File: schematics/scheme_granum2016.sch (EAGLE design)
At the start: 42 parts, among them M1 SMALL_SERVO, U1 TSL2561T, U2 TSL2561T, U3 TSL2561T

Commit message: добавляем в пояснительную записку описание измерительного моста + в схеме подключен мост, термисторы и немного по мелочам Гранум, с наступающим!
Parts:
- removed LSP10, LSP12, LSP13, LSP14, LSP15, LSP16, LSP2, LSP3, LSP4, LSP8, LSP9: LSP10, solpad:LSP10
- removed R8, R9: PTC-SOD70, ptc-ntc:PTC-SOD70
- removed X2: (no value), con-molex:KK-156-8
- added 3.3V_1, 5V_1, 5V_2, 5V_3, ADDR_LS1, ADDR_LS2, ADDR_LS3, BZZR, CMN1, CMN2, CMN3, CS_ADXL, CS_DP, DHT, EN_MP1, EN_MP2, EN_MP3, GND1_1, GND2_2, GND3_3, INT1, INT2, INT_LS1, INT_LS2, INT_LS3, NTC1, NTC2, NTC3, SCL, SDA, SERVO, SOIL1, SOIL2: LSP10, solpad:LSP10
- added R11, R13: PTC-SOD70, ptc-ntc:PTC-SOD70
- added R12, R14: (no value), eagle-ltspice:R0207/10
- renumbered LSP5 to CS_MP1, LSP6 to CS_MP2, LSP7 to CS_MP3
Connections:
- removed net N$9: U3.VDD
- new net +3V3: U$1.VIO, U$1.VS, U$2.VDD, U$7.VDD, U1.VDD, U2.VDD, U3.VDD
- new net +5V: M1.V+, U$3.VCC, U$3.VH/RH, U$4.VCC, U$4.Y0, U$5.VCC, U$5.Y0, U$6.VCC, U$6.Y0, U4.VDD
- new net 3.3V_1: 3.3V_1.MP
- new net 5V_1: 5V_1.MP, R12.1, R14.1, R5.1
- new net 5V_2: 5V_2.MP
- new net 5V_3: 5V_3.MP
- new net GND1: GND1_1.MP, R10.1
- new net GND2: GND2_2.MP, R11.1
- new net GND3: GND3_3.MP, R13.1
- new net N$22: R6.2, SOIL1.MP, U$4.Y1, U$5.Y1, U$6.Y1
- new net N$24: CMN1.MP, U$5.Z
- new net N$26: NTC2.MP, R12.2, U$7.A1
- new net N$28: R7.2, SOIL2.MP, U$3.VW/RW
- new net N$30: NTC3.MP, R14.2, U$7.A2
- new net N$31: CMN2.MP, U$6.Z
- new net N$32: CMN3.MP, U$4.Z
- net 3.3V: no longer U$2.VDD, U1.VDD, U2.VDD
- net 5V: no longer M1.V+, U4.VDD
- net GND: now also R6.1, R7.1, U$3.VL/RL, U$3.VSS
- net N$13: now also EN_MP2.MP; no longer LSP9.MP
- net N$14: now also EN_MP3.MP; no longer LSP10.MP
- net N$16: now also EN_MP1.MP; no longer LSP8.MP
- net N$17: now also INT_LS3.MP; no longer LSP12.MP
- net N$18: now also BZZR.MP
- net N$19: now also DHT.MP
- net N$2: now also INT1.MP; no longer LSP3.MP
- net N$20: now also NTC1.MP, R5.2, U$7.A0; no longer U$7.VDD
- net N$21: now also INT_LS2.MP; no longer LSP15.MP
- net N$23: now also ADDR_LS2.MP; no longer LSP13.MP
- net N$25: now also SERVO.MP
- net N$27: now also INT_LS1.MP; no longer LSP16.MP
- net N$29: now also ADDR_LS1.MP; no longer LSP14.MP
- net N$3: now also SCL.MP; no longer X2-1.S
- net N$4: now also INT2.MP; no longer LSP2.MP
- net N$5: now also CS_DP.MP, U$3.CS; no longer U$1.CS, U$1.VIO, U$1.VS
- net N$6: now also ADDR_LS3.MP; no longer LSP4.MP
- net N$7: now also SDA.MP; no longer X2-2.S
- net N$8: now also CS_ADXL.MP, U$1.CS; no longer U$4.VCC, U$5.VCC, U$6.VCC
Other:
- moved on the sheet: LSP1, LSP11, R10, R5, R6, R7, SG1, U1, U2, U3, U4

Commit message: в ПЗ добавлено описание измерения твердости, в презентации изменено расширение видео, в схемах теперь подключены STM32, microSD & GPS, в библиотеке есть ATmega128
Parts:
- removed 5V_1, 5V_2, 5V_3, GND3_3: LSP10, solpad:LSP10
- added 3.3V_2, 3.3V_3, 5V_1_1, 5V_1_2, 5V_2_1, 5V_2_2, 5V_3_1, 5V_3_2, GND1_2, GND2_1, GND3_1, GND3_2: LSP10, solpad:LSP10
- added U$10: MICRO_SD, elements_cs2016:MICRO_SD
- added U$11: ATMEGA128, elements_cs2016:ATMEGA128
- added U$8: STM32, elements_cs2016:STM32
- added U$9: GPS, elements_cs2016:GPS
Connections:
- removed net +3V3: U$1.VIO, U$1.VS, U$2.VDD, U$7.VDD, U1.VDD, U2.VDD, U3.VDD
- removed net 5V_1: 5V_1.MP, R12.1, R14.1, R5.1
- removed net 5V_2: 5V_2.MP
- removed net 5V_3: 5V_3.MP
- removed net GND1: GND1_1.MP, R10.1
- removed net GND2: GND2_2.MP, R11.1
- removed net GND3: GND3_3.MP, R13.1
- new net 3.3V_2: 3.3V_2.MP, U$1.SDO, U$1.VIO, U$1.VS, U$7.VDD, U2.VDD
- new net 3.3V_3: 3.3V_3.MP, U$8.3.3V, U$9.VCC, U1.VDD
- new net 5V11: 5V_1_1.MP, R5.1
- new net 5V12: 5V_1_2.MP
- new net 5V21: 5V_2_1.MP, R12.1, U4.VDD
- new net 5V22: 5V_2_2.MP, M1.V+
- new net 5V31: 5V_3_1.MP, R14.1, U$8.5V
- new net 5V32: 5V_3_2.MP, U$10.VCC
- new net GND11: GND1_1.MP, R10.1, U$2.GND
- new net GND12: GND1_2.MP, SG1.-, U3.GND
- new net GND21: GND2_1.MP, M1.GND, R11.1, U$1.GND, U$11.GND1, U$11.GND2, U4.GND
- new net GND22: GND2_2.MP, U$11.GND, U$7.GND, U2.GND
- new net GND31: GND3_1.MP, R13.1, U$10.GND, U$8.G, U$8.GN, U$8.GNDD, U$9.GND
- new net GND32: GND3_2.MP, U1.GND
- new net N$33: U$8.B6, U$9.RX
- new net N$34: U$10.MISO, U$8.A6
- new net N$35: U$10.MOSI, U$8.A7
- new net N$36: U$10.SCK, U$8.A5
- new net N$37: U$10.CS, U$8.A4
- new net N$9: U$8.B7, U$9.TX
- new net SCL: SCL.MP, U$11.(SCL/INT0)PD0, U2.SCL, U3.SCL
- new net SDA: SDA.MP, U$11.(SDA/INT1)PD1, U2.SDA, U3.SDA
- new net SDA_3,3V: U$1.SDA
- net +5V: no longer M1.V+, U4.VDD
- net 3.3V: no longer U$1.SDO
- net 3.3V_1: now also U$2.VDD, U3.VDD
- net GND: no longer M1.GND, SG1.-, U$1.GND, U$2.GND, U$7.GND, U1.GND, U2.GND, U3.GND, U4.GND
- net N$3: no longer SCL.MP
- net N$7: no longer SDA.MP
- net SCL_3.3V: no longer U3.SCL
- net SCL_5V: no longer U2.SCL
- net SDA_3.3V: now also Q2.S, R4.1; no longer U$1.SDA, U3.SDA
- net SDA_5V: no longer Q2.S, R4.1, U2.SDA
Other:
- moved on the sheet: 3.3V_1, CMN1, CMN2, CMN3, CS_ADXL, CS_DP, CS_MP1, CS_MP2, CS_MP3, DHT, EN_MP1, EN_MP2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

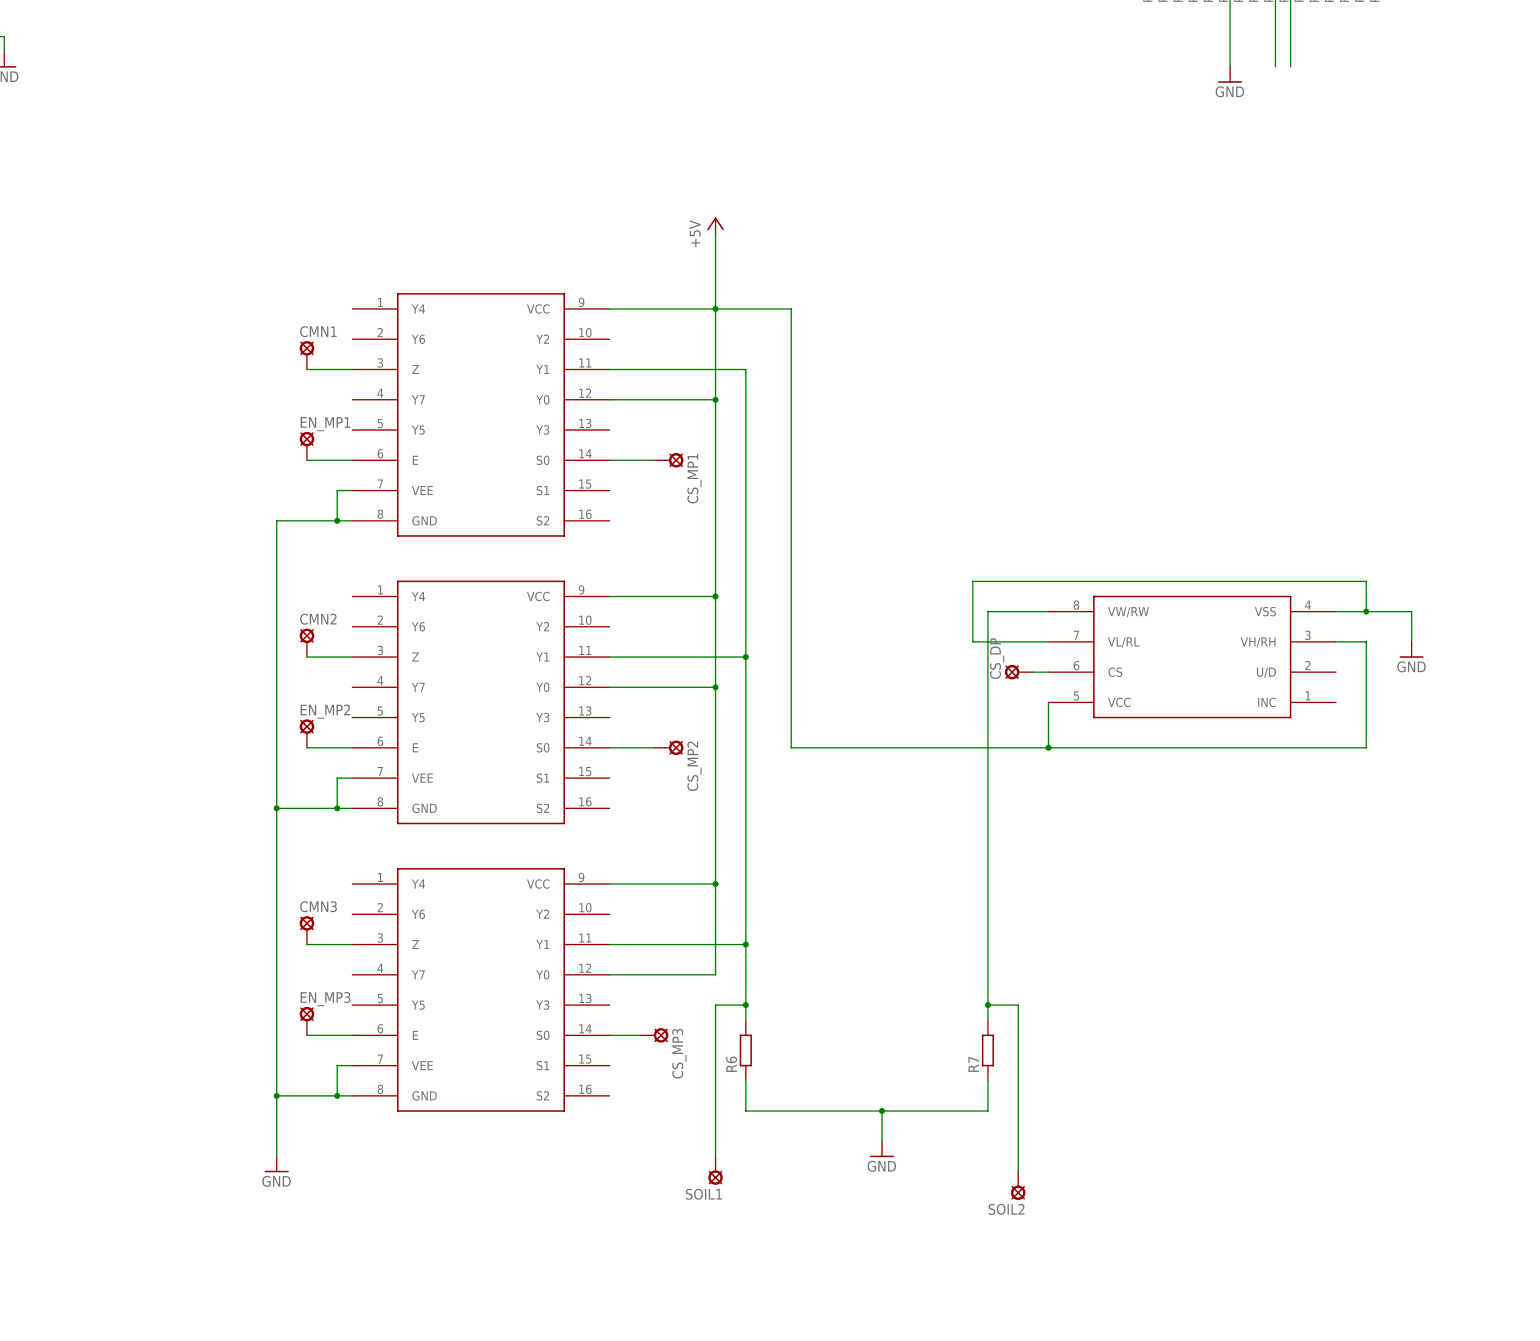
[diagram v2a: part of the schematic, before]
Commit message: подправила мостовую схему
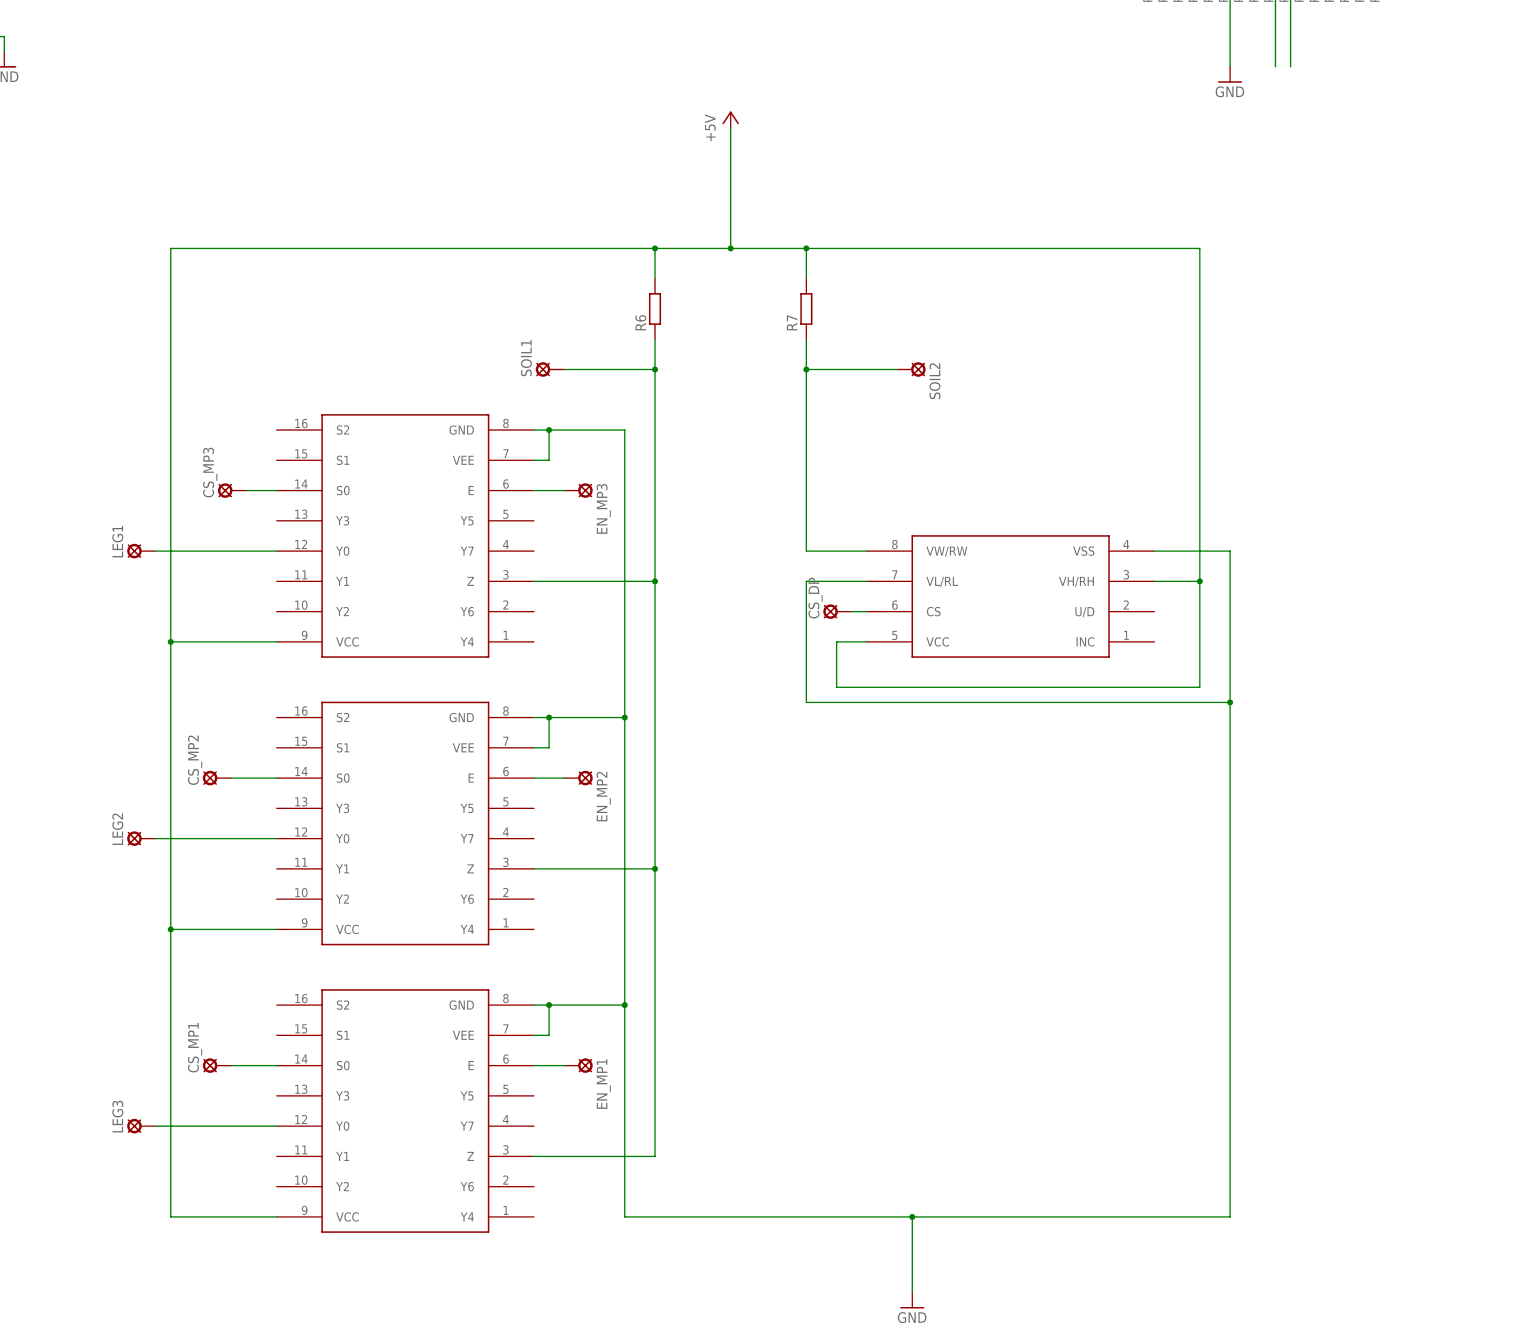
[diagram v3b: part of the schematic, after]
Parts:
- removed CMN1, CMN2, CMN3: LSP10, solpad:LSP10
- added LEG1, LEG2, LEG3: LSP10, solpad:LSP10
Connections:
- removed net +5V: U$3.VCC, U$3.VH/RH, U$4.VCC, U$4.Y0, U$5.VCC, U$5.Y0, U$6.VCC, U$6.Y0
- removed net GND: R6.1, R7.1, U$3.VL/RL, U$3.VSS, U$4.GND, U$4.VEE, U$5.GND, U$5.VEE, U$6.GND, U$6.VEE
- removed net N$24: CMN1.MP, U$5.Z
- removed net N$31: CMN2.MP, U$6.Z
- removed net N$32: CMN3.MP, U$4.Z
- new net N$38: R7.1, SOIL2.MP, U$3.VW/RW
- new net N$41: LEG2.MP, U$6.Y0
- new net N$42: LEG1.MP, U$4.Y0
- net 5V11: now also R6.2, R7.2, U$3.VCC, U$3.VH/RH, U$4.VCC, U$5.VCC, U$6.VCC
- net GND11: now also U$3.VL/RL, U$3.VSS, U$4.GND, U$4.VEE, U$5.GND, U$5.VEE, U$6.GND, U$6.VEE
- net N$22: now also LEG3.MP, U$5.Y0; no longer R6.2, SOIL1.MP, U$4.Y1, U$5.Y1, U$6.Y1
- net N$28: now also R6.1, SOIL1.MP, U$4.Z, U$5.Z, U$6.Z; no longer R7.2, SOIL2.MP, U$3.VW/RW
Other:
- moved on the sheet: CS_DP, CS_MP1, CS_MP2, CS_MP3, EN_MP1, EN_MP2, EN_MP3, R6, R7, SOIL1, SOIL2

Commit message: финальные этапы в разработке принципиальной ЭС. изменен измерительный мост, добавлены выводы для контрольно-испытательной аппаратуры, а вся аппаратура подключена к МК
Удалены лишние файлы
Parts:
- removed ADDR_LS1, ADDR_LS2, ADDR_LS3, BZZR, CS_ADXL, CS_DP, CS_MP1, CS_MP2, CS_MP3, DHT, EN_MP1, EN_MP2, EN_MP3, INT1, INT2, INT_LS1, INT_LS2, INT_LS3, LSP1, LSP11, SCL, SDA, SERVO, SOIL1, SOIL2: LSP10, solpad:LSP10
- removed Q1, Q2: (no value), transistors:2N7002_SOT23
- removed R1, R2, R3, R4: (no value), eagle-ltspice:R0207/10
- removed U$4: 74HC4051, elements_cs2016:74HC4051
- added SCL1, SCL3, SDA1, SDA3: LSP10, solpad:LSP10
- added X1, X2: 1365-10, con-leotronics:1365-10
- U$2: value ADS1115 -> DS18B20; device elements_cs2016:ADS1115 -> elements_cs2016:DS18B20
- U$3: value X9C104 -> MCP42100; device elements_cs2016:X9C104 -> elements_cs2016:MCP42100
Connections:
- removed net 3.3V: Q1.G, Q2.G, R2.2, R4.2
- removed net 5V: R1.2, R3.2
- removed net N$28: R6.1, SOIL1.MP, U$4.Z, U$5.Z, U$6.Z
- removed net N$29: ADDR_LS1.MP, U1.ADDR
- removed net N$33: U$8.B6, U$9.RX
- removed net N$34: U$10.MISO, U$8.A6
- removed net N$38: R7.1, SOIL2.MP, U$3.VW/RW
- removed net N$42: LEG1.MP, U$4.Y0
- removed net SCL: SCL.MP, U$11.(SCL/INT0)PD0, U2.SCL, U3.SCL
- removed net SCL_3.3V: Q1.S, R2.1, U$1.SCL, U$2.SCL, U$7.SCL
- removed net SCL_5V: U1.SCL
- removed net SDA: SDA.MP, U$11.(SDA/INT1)PD1, U2.SDA, U3.SDA
- removed net SDA_3,3V: U$1.SDA
- removed net SDA_3.3V: Q2.S, R4.1, U$2.SDA, U$7.SDA
- removed net SDA_5V: U1.SDA
- new net +5V: U$2.VDD
- new net GND: U$11.GND1, U$11.GND2, U$2.GND
- new net MISO: U$10.MISO, U$11.(MISO)PB3, U$3.SO, U$8.B14, X1-9.S
- new net MOSI: U$10.MOSI, U$11.(MOSI)PB2, U$3.SI, U$8.B15, X1-7.S
- new net N$32: U$11.(OC1B)PB6, U$3.CS
- new net N$39: X2-4.S
- new net N$40: X2-6.S
- new net N$44: X1-8.S
- new net N$45: X1-10.S
- new net RX0: X2-1.S
- new net RX1: X2-5.S
- new net RX2: U$8.B6, U$9.RX, X1-4.S
- new net SCK: U$10.SCK, U$11.(SCK)PB1, U$3.SCK, U$8.B13, X1-5.S
- new net SCL1: SCL1.MP, U3.SCL, X1-3.S
- new net SCL2: U$11.(SCL/INT0)PD0, U$7.SCL, U2.SCL
- new net SCL3: SCL3.MP, U1.SCL
- new net SDA1: SDA1.MP, U3.SDA, X1-1.S
- new net SDA2: U$11.(SDA/INT1)PD1, U$7.SDA, U2.SDA
- new net SDA3: SDA3.MP, U1.SDA
- new net SOIL1: R6.1, U$11.PA2(AD2), U$6.Z
- new net SOIL2: R7.1, U$11.PA3(AD3), U$3.PW0
- new net TX0: X2-3.S
- new net TX1: X2-7.S
- new net TX2: U$8.B7, U$9.TX, X1-6.S
- net 3.3V_1: now also U3.ADDR; no longer U$2.VDD
- net 3.3V_2: no longer U$1.SDO
- net 5V11: now also M1.V+, U$3.RS, U$3.SHDN, U$3.VDD; no longer U$3.VCC, U$3.VH/RH, U$4.VCC
- net 5V22: now also U$11.VCC, U$11.VCC1; no longer M1.V+
- net GND11: now also U$3.PB0, U$5.S0, U$5.Z, U$6.S0; no longer U$2.GND, U$3.VL/RL, U$4.GND, U$4.VEE
- net GND12: now also M1.GND; no longer SG1.-
- net GND21: now also SG1.-, X1-2.S, X2-10.S; no longer M1.GND, U$11.GND1, U$11.GND2
- net GND22: now also U2.ADDR
- net GND31: no longer U$8.G, U$8.GN
- net GND32: now also U$8.G, U$8.GN
- net N$1: now also U$11.(OC1A)PB5, U$8.B12; no longer LSP1.MP, U$2.ADDR
- net N$10: now also U$11.PA5(AD5), U$5.S2; no longer CS_MP1.MP, U$5.S0
- net N$11: now also U$11.PA4(AD4), U$5.S1; no longer CS_MP2.MP, U$6.S0
- net N$12: now also LEG3.MP, U$5.Y2, U$6.Y2; no longer CS_MP3.MP, U$4.S0
- net N$13: now also U$11.PA0(AD0); no longer EN_MP2.MP
- net N$14: now also LEG1.MP, U$5.Y0, U$6.Y0; no longer EN_MP3.MP, U$4.E
- net N$15: now also U$11.PA6(AD6); no longer LSP11.MP
- net N$16: now also U$11.PA1(AD1); no longer EN_MP1.MP
- net N$17: now also U$11.(OC3B/INT4)PE4; no longer INT_LS3.MP
- net N$18: now also U$1.SDO, U$8.A6; no longer BZZR.MP, SG1.+
- net N$19: now also U$11.(T2)PD7; no longer DHT.MP
- net N$2: now also U$1.INT1, U$8.A0; no longer INT1.MP, U$1.INT2
- net N$21: now also U$11.(OC3C/INT5)PE5; no longer INT_LS2.MP
- net N$22: now also LEG2.MP, U$5.Y1, U$6.Y1; no longer LEG3.MP, U$5.Y0
- net N$23: now also U$1.SDA, U$8.A7; no longer ADDR_LS2.MP, U2.ADDR
- net N$25: now also U$11.(XCK1)PD5; no longer SERVO.MP
- net N$27: now also U$11.(T3/INT6)PE6; no longer INT_LS1.MP
- net N$3: now also U$10.CS, U$11.(OC0)PB4; no longer Q1.D, R3.1
- net N$35: now also X2-9.S; no longer U$10.MOSI, U$8.A7
- net N$36: now also SG1.+, U$11.(T1)PD6; no longer U$10.SCK, U$8.A5
- net N$37: now also X2-2.S; no longer U$10.CS, U$8.A4
- net N$4: now also U$1.INT2, U$8.A1; no longer INT2.MP, U$1.INT1
- net N$41: now also X2-8.S; no longer LEG2.MP, U$6.Y0
- net N$5: now also U$11.(XCK0/AIN0)PE2, U$6.S1; no longer CS_DP.MP, U$3.CS
- net N$6: now also U$8.A4; no longer ADDR_LS3.MP, U3.ADDR
- net N$7: now also U$11.(OC3A/AIN1)PE3, U$6.S2; no longer Q2.D, R1.1
- net N$8: now also U$1.SCL, U$8.A5; no longer CS_ADXL.MP, U$1.CS
- net N$9: now also U$11.(OC2/OC1C)PB7, U$2.DQ; no longer U$8.B7, U$9.TX
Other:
- note removed: "SCL3.3"
- note removed: "SDA3.3"
- note removed: "VCC3.3"
- note removed: "VCC5"
- moved on the sheet: 3.3V_1, 3.3V_2, 3.3V_3, 5V_1_1, 5V_1_2, 5V_2_1, 5V_2_2, 5V_3_1, 5V_3_2, GND1_1, GND1_2, GND2_1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
